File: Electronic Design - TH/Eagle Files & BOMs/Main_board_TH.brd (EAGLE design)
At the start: 90 x 60 mm, 46 parts, among them IC2 ATMEGA328-PU, X1 16MHz

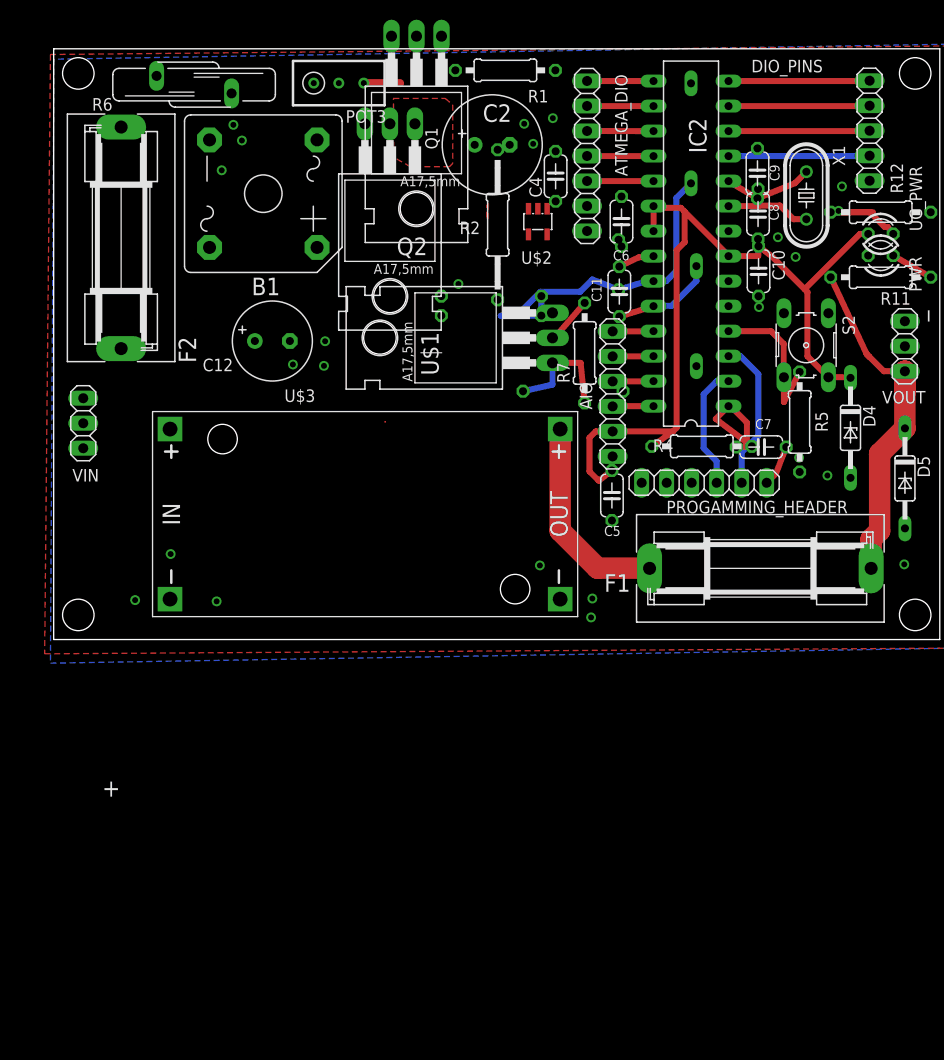
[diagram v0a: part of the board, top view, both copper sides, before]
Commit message: renamed files to reflect two versions of L.E.One and replacing ATmega 328 with arduino nano
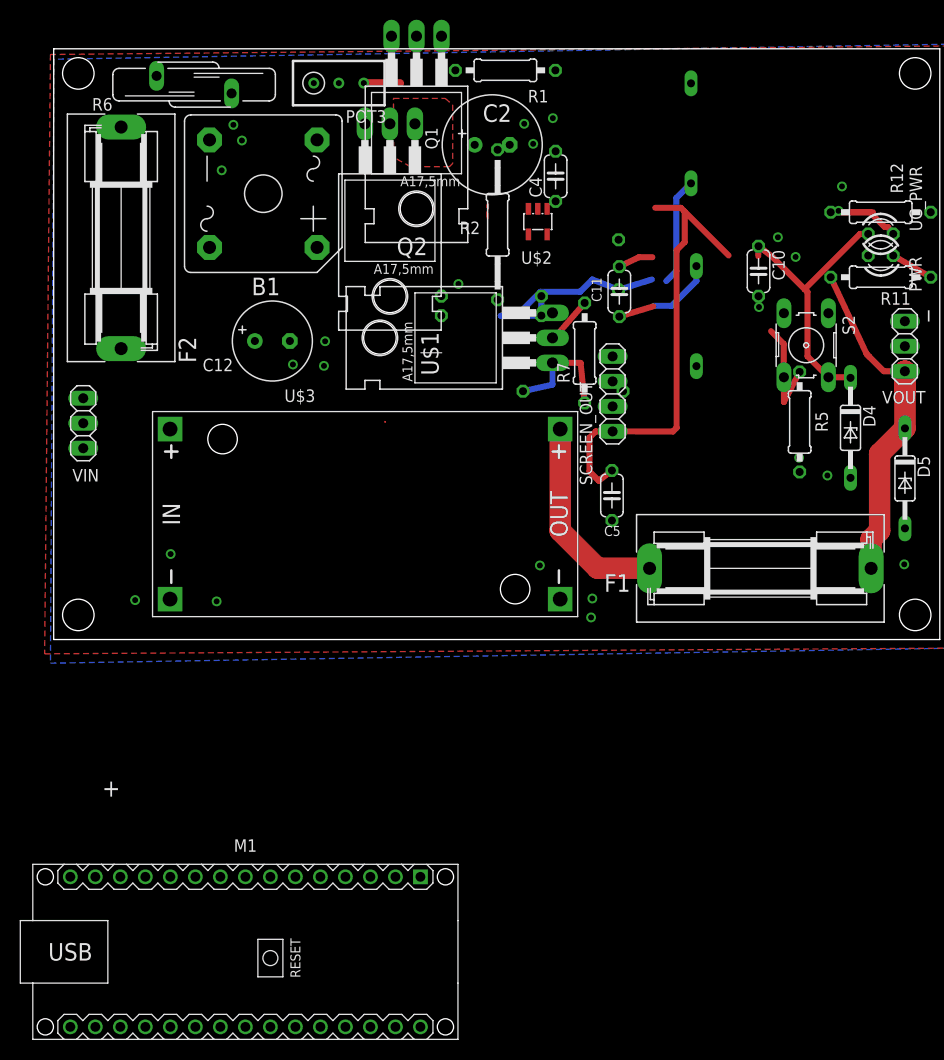
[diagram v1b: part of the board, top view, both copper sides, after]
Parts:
- removed AIO, PROGAMMING_HEADER: (no value), pinhead:1X06
- removed ATMEGA_DIO: (no value), pinhead:1X07
- removed C6, C7: 0.1u, resistor:C050-024X044
- removed C8, C9: 22p, resistor:C050-024X044
- removed DIO_PINS: (no value), pinhead:1X05
- removed IC2: ATMEGA328-PU, Arduino-AVR:DIL28-3
- removed R4: 10k, resistor:0207/10
- removed X1: 16MHz, crystal:HC49/S
- added M1: ARDUINO-NANO-3.0, diy-modules:ARDUINO-NANO-3.0
- added SCREEN_OUT: (no value), pinhead:1X04
- C10: value 0.1u -> 10u
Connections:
- removed net ANALOG_2: AIO.1, IC2.25
- removed net ANALOG_3: AIO.2, IC2.26
- removed net ANALOG_4: AIO.3, IC2.27
- removed net ANALOG_5: AIO.4, IC2.28
- removed net CRYSTAL1: C8.1, IC2.9, X1.2
- removed net CRYSTAL2: C9.1, IC2.10, X1.1
- removed net D10: ATMEGA_DIO.2, IC2.16
- removed net D11: ATMEGA_DIO.3, IC2.17
- removed net D12: ATMEGA_DIO.4, IC2.18
- removed net D13: ATMEGA_DIO.5, IC2.19
- removed net D5: DIO_PINS.2, IC2.11
- removed net D6: DIO_PINS.3, IC2.12
- removed net D7: DIO_PINS.4, IC2.13
- removed net D8: DIO_PINS.5, IC2.14
- removed net D9: ATMEGA_DIO.1, IC2.15
- removed net N$14: C7.2, PROGAMMING_HEADER.1
- removed net N$4: IC2.3, PROGAMMING_HEADER.2
- removed net N$5: IC2.2, PROGAMMING_HEADER.3
- removed net RESET: C7.1, IC2.1, R4.2
- new net 3V3: M1.J2.14
- new net 5V: M1.J2.4
- new net A2: M1.J2.10
- new net A3: M1.J2.9
- new net A6: M1.J2.6
- new net A7: M1.J2.5
- new net GND.1: M1.J1.4
- new net GND.2: M1.J2.2
- new net N$2: M1.J2.8, SCREEN_OUT.2
- new net N$3: M1.J2.7, SCREEN_OUT.1
- net +5V: now also M1.J2.1, SCREEN_OUT.3; no longer AIO.5, ATMEGA_DIO.6, C6.1, IC2.20, IC2.21, IC2.7, R4.1
- net BUTTON: now also M1.J1.5; no longer IC2.4
- net GND: now also SCREEN_OUT.4; no longer AIO.6, ATMEGA_DIO.7, C6.2, C8.2, C9.2, DIO_PINS.1, IC2.22, IC2.8, PROGAMMING_HEADER.6
- net IIN: no longer IC2.24
- net VIN: no longer IC2.23
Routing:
- net N$4: track 15.5 -> 0.00 mm
- net D7: track 14.3 -> 0.00 mm
- net D6: track 14.3 -> 0.00 mm
- net D5: track 14.3 -> 0.00 mm
- net D8: track 14.3 -> 0.00 mm
- net N$5: track 12.6 -> 0.00 mm
- net RESET: track 12.5 -> 0.00 mm
- net CRYSTAL1: track 11.6 -> 0.00 mm
- net CRYSTAL2: track 9.18 -> 0.00 mm
- net +5V: track 90.0 -> 80.9 mm
- net D11: track 6.96 -> 0.00 mm
- net D10: track 6.95 -> 0.00 mm
- net D13: track 6.95 -> 0.00 mm
- net D12: track 6.95 -> 0.00 mm
- net D9: track 6.75 -> 0.00 mm
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
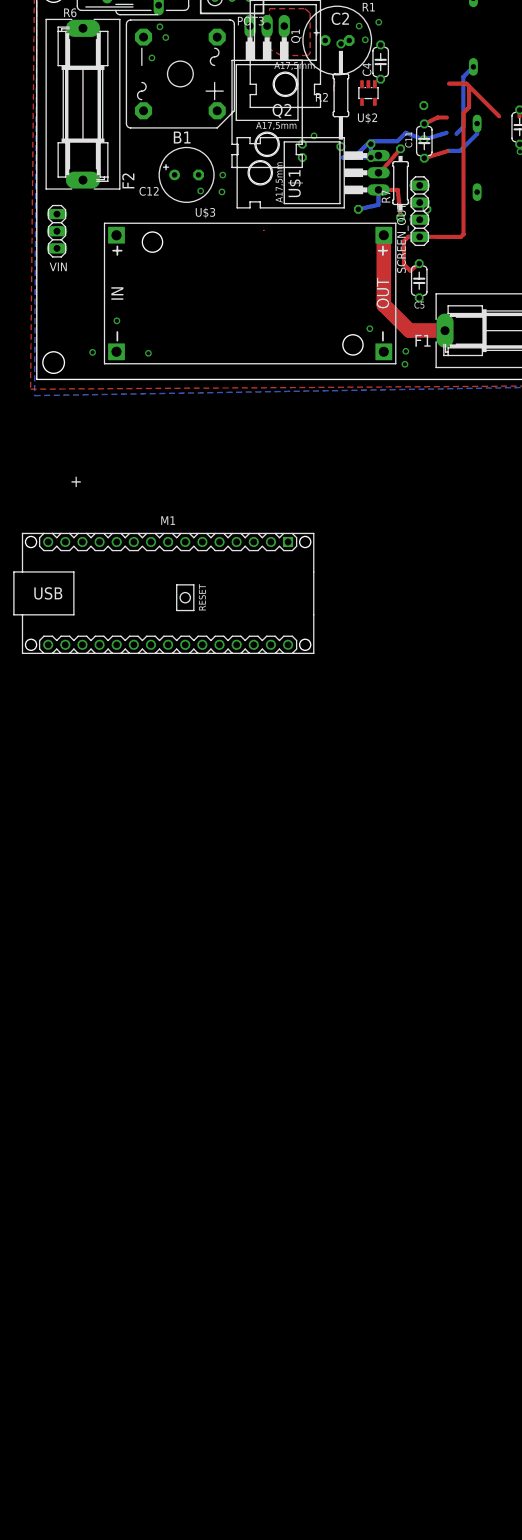
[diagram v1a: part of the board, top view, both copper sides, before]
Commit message: replacing CS30 with LM358
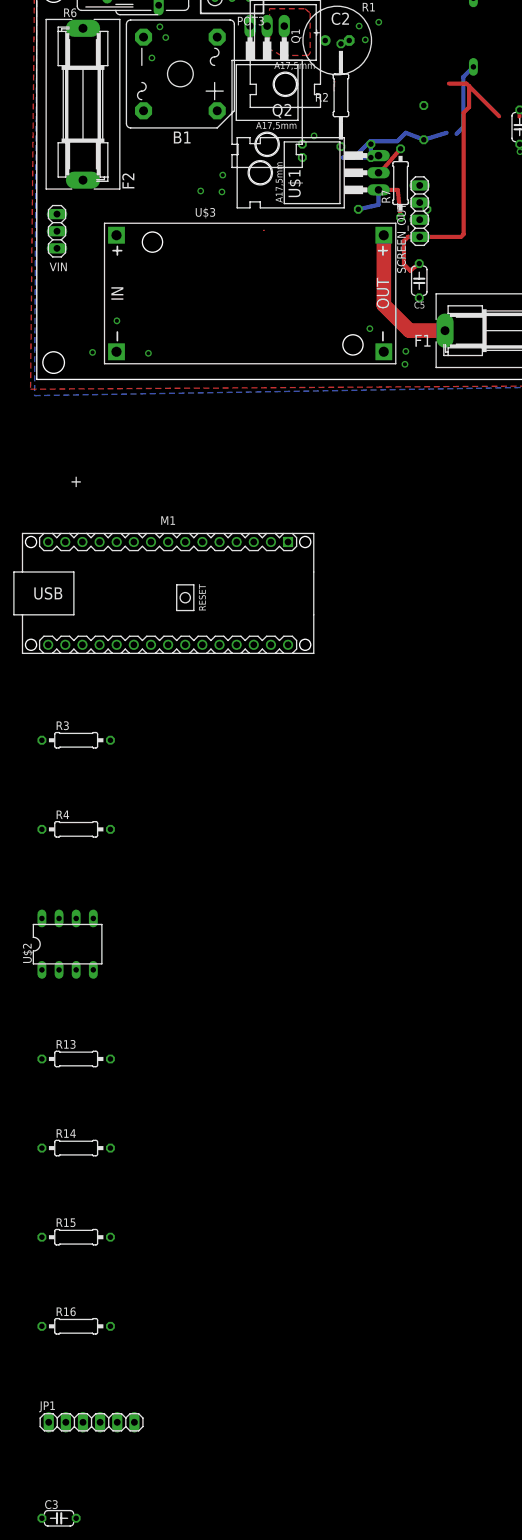
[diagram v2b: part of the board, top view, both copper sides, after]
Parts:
- removed C11: 10n, resistor:C050-024X044
- removed C12: 100uF, resistor:E3,5-8
- removed C4: 0.1u, resistor:C050-024X044
- removed D3: 5.1V, diode:DO35Z10
- added C3: 10u, resistor:C050-024X044
- added JP1: (no value), pinhead:1X06
- added R13, R16: 47k, resistor:0207/10
- added R14, R15: 10k, resistor:0207/10
- added R3, R4: 1k, resistor:0207/10
- R7: value 1k -> 220R
- R8: value 3k -> 680R
- U$2: value CS30 -> LM358; device Samson:SOT23-5L -> Samson:DIL08
- moved U$2 133.8 mm to (4.57, -83.7), turned to 0 degrees
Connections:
- removed net VIN_CURRENT_MEASURED: C12.+, R2.2, R9.2, U$1.3, U$2.4, U$3.IN+
- new net N$4: R2.2, R4.2, U$3.IN-
- new net N$5: R16.1, R4.1, U$2.3
- new net N$6: R13.2, R3.1, U$2.2
- new net N$8: R14.2, R15.1, R16.2
- net +5V: now also R15.2; no longer C4.1, U$2.5
- net A2: now also JP1.1
- net A3: now also JP1.2
- net A6: now also JP1.3
- net A7: now also JP1.4
- net GND: now also C3.2, JP1.5, JP1.6, R14.1, R2.1, R3.2, U$2.4; no longer C11.2, C12.-, C4.2, D3.A, U$2.2, U$3.IN-
- net IIN: now also M1.J2.12, R13.1; no longer C11.1, D3.C
- net VIN: now also M1.J2.11
- net VIN_PROTECTED: now also C3.1, R9.2, U$1.3, U$2.7, U$3.IN+; no longer R2.1, U$2.3
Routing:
- net IIN: track 10.5 -> 0.00 mm
- net GND: track 3.57 -> 0.00 mm

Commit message: replacing divider resistors for voltage measurement
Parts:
- R10: value 1k13 -> 1k
- R9: value 21k5 -> 10k
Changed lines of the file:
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@@
 <attribute name="VALUE" x="54.6" y="16.23" size="1.016" layer="27" rot="R270"/>
 </element>
-<element name="R9" library="resistor" package="0207/10" value="21k5" x="44.45" y="34.88" rot="MR0"/>
-<element name="R10" library="resistor" package="0207/10" value="1k13" x="44.45" y="32.9" rot="MR180"/>
+<element name="R9" library="resistor" package="0207/10" value="10k" x="44.45" y="34.88" rot="MR0"/>
+<element name="R10" library="resistor" package="0207/10" value="1k" x="44.45" y="32.9" rot="MR180"/>
 <element name="D4" library="diode" package="DO35Z10" value="5.1V" x="80.93" y="21.5" rot="R270"/>
 <element name="D5" library="diode" package="DO35Z10" value="5.1V" x="86.46" y="16.37" rot="R270"/>

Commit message: Adding names of Q1 and Q2
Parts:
- Q1, Q2: value (none) -> IRF9520
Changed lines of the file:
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@@
 <attribute name="VALUE" x="85.27" y="45.94" size="1.27" layer="27" rot="R180"/>
 </element>
-<element name="Q1" library="Samson" package="TO220BH" value="" x="36.85" y="54.93" smashed="yes" rot="R180">
+<element name="Q1" library="Samson" package="TO220BH" value="IRF9520" x="36.85" y="54.93" smashed="yes" rot="R180">
 <attribute name="NAME" x="37.735" y="52.015" size="1.27" layer="25" rot="R270"/>
 <attribute name="VALUE" x="39.055" y="58.755" size="1.27" layer="27" rot="R180"/>
 </element>
-<element name="Q2" library="Samson" package="TO220BH" value="" x="34.15" y="46.03" rot="R180"/>
+<element name="Q2" library="Samson" package="TO220BH" value="IRF9520" x="34.15" y="46.03" rot="R180"/>
 <element name="F2" library="fuse" package="SH22,5A" value="FUSESH22,5A" x="6.85" y="40.8" rot="R90">
 <attribute name="MF" value="" x="6.85" y="40.8" size="1.778" layer="27" rot="R90" display="off"/>

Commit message: adding ground to arduino
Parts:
- moved U$2 102.0 mm to (-3.81, -185.3)
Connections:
- removed net GND.2: M1.J2.2
- net GND: now also M1.J2.2
- net VIN_PROTECTED: now also U$2.8; no longer U$2.7
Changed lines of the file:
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@@
 <element name="R3" library="resistor" package="0207/10" value="1k" x="5.84" y="-53.49"/>
 <element name="R4" library="resistor" package="0207/10" value="1k" x="5.84" y="-66.7"/>
-<element name="U$2" library="Samson" package="DIL08" value="LM358" x="4.57" y="-83.72"/>
+<element name="U$2" library="Samson" package="DIL08" value="LM358" x="-3.81" y="-185.34"/>
 <element name="R13" library="resistor" package="0207/10" value="47k" x="5.84" y="-100.74"/>
 <element name="R14" library="resistor" package="0207/10" value="10k" x="5.84" y="-113.95"/>
@@
 <contactref element="JP1" pad="6"/>
 <contactref element="C3" pad="2"/>
+<contactref element="M1" pad="J2.2"/>
+<wire x1="5.84" y1="-168.83" x2="0" y2="-189.15" width="0" layer="19" extent="1-1"/>
 <wire x1="11.93" y1="-154.6" x2="5.84" y2="-168.83" width="0" layer="19" extent="1-1"/>
 <wire x1="14.47" y1="-154.6" x2="11.93" y2="-154.6" width="0" layer="19" extent="1-1"/>
 <wire x1="0.76" y1="-113.95" x2="11.93" y2="-154.6" width="0" layer="19" extent="1-1"/>
-<wire x1="8.38" y1="-87.53" x2="0.76" y2="-113.95" width="0" layer="19" extent="1-1"/>
-<wire x1="10.92" y1="-53.49" x2="8.38" y2="-87.53" width="0" layer="19" extent="1-1"/>
-<wire x1="8.2698" y1="4.00569375" x2="10.92" y2="-53.49" width="0" layer="19" extent="1-1"/>
-<wire x1="11.8798" y1="8.68569375" x2="8.2698" y2="4.00569375" width="0" layer="19" extent="1-1"/>
-<wire x1="16.5498" y1="3.87569375" x2="11.8798" y2="8.68569375" width="0" layer="19" extent="1-1"/>
-<wire x1="24.2998" y1="27.93569375" x2="11.8798" y2="8.68569375" width="0" layer="19" extent="1-1"/>
-<wire x1="27.4498" y1="27.79569375" x2="24.2998" y2="27.93569375" width="0" layer="19" extent="1-1"/>
-<wire x1="27.5698" y1="30.29569375" x2="27.4498" y2="27.79569375" width="0" layer="19" extent="1-1"/>
-<wire x1="39.37" y1="32.9" x2="27.5698" y2="30.29569375" width="0" layer="19" extent="1-1"/>
-<wire x1="41.10569375" y1="36.1102" x2="39.37" y2="32.9" width="0" layer="19" extent="1-1"/>
-<wire x1="45.09" y1="49.75" x2="41.10569375" y2="36.1102" width="0" layer="19" extent="1-1"/>
-<wire x1="46.319284375" y1="50.247296875" x2="45.09" y2="49.75" width="0" layer="19" extent="1-1"/>
-<wire x1="48.6998" y1="50.34569375" x2="46.319284375" y2="50.247296875" width="0" layer="19" extent="1-1"/>
+<wire x1="10.92" y1="-53.49" x2="0.76" y2="-113.95" width="0" layer="19" extent="1-1"/>
+<wire x1="34.71" y1="-39.34" x2="10.92" y2="-53.49" width="0" layer="19" extent="1-1"/>
+<wire x1="54.5798" y1="2.24569375" x2="34.71" y2="-39.34" width="0" layer="19" extent="1-1"/>
+<wire x1="54.7098" y1="4.16569375" x2="54.5798" y2="2.24569375" width="0" layer="19" extent="1-1"/>
+<wire x1="51.442" y1="4.104" x2="54.7098" y2="4.16569375" width="0" layer="19" extent="1-1"/>
+<wire x1="49.3798" y1="7.52569375" x2="51.442" y2="4.104" width="0" layer="19" extent="1-1"/>
+<wire x1="56.7" y1="12.09" x2="54.7098" y2="4.16569375" width="0" layer="19" extent="1-1"/>
+<wire x1="56.77" y1="21.14" x2="56.7" y2="12.09" width="0" layer="19" extent="1-1"/>
+<wire x1="57.83" y1="25.22" x2="56.77" y2="21.14" width="0" layer="19" extent="1-1"/>
+<wire x1="57.373834375" y1="40.608153125" x2="57.83" y2="25.22" width="0" layer="19" extent="1-1"/>
+<wire x1="48.6998" y1="50.34569375" x2="57.373834375" y2="40.608153125" width="0" layer="19" extent="1-1"/>
 <wire x1="47.7898" y1="52.38569375" x2="48.6998" y2="50.34569375" width="0" layer="19" extent="1-1"/>
+<wire x1="46.319284375" y1="50.247296875" x2="48.6998" y2="50.34569375" width="0" layer="19" extent="1-1"/>
+<wire x1="45.09" y1="49.75" x2="46.319284375" y2="50.247296875" width="0" layer="19" extent="1-1"/>
 <wire x1="50.6998" y1="52.95569375" x2="47.7898" y2="52.38569375" width="0" layer="19" extent="1-1"/>
 <wire x1="50.95703125" y1="57.813271875" x2="50.6998" y2="52.95569375" width="0" layer="19" extent="1-1"/>
-<wire x1="57.373834375" y1="40.608153125" x2="48.6998" y2="50.34569375" width="0" layer="19" extent="1-1"/>
 <wire x1="64.7298" y1="56.4956875" x2="50.95703125" y2="57.813271875" width="0" layer="19" extent="1-1"/>
+<wire x1="41.10569375" y1="36.1102" x2="45.09" y2="49.75" width="0" layer="19" extent="1-1"/>
+<wire x1="39.37" y1="32.9" x2="41.10569375" y2="36.1102" width="0" layer="19" extent="1-1"/>
+<wire x1="27.5698" y1="30.29569375" x2="39.37" y2="32.9" width="0" layer="19" extent="1-1"/>
+<wire x1="27.4498" y1="27.79569375" x2="27.5698" y2="30.29569375" width="0" layer="19" extent="1-1"/>
+<wire x1="24.2998" y1="27.93569375" x2="27.4498" y2="27.79569375" width="0" layer="19" extent="1-1"/>
 <wire x1="71.59" y1="34.87" x2="57.373834375" y2="40.608153125" width="0" layer="19" extent="1-1"/>
 <wire x1="71.63569375" y1="33.7702" x2="71.59" y2="34.87" width="0" layer="19" extent="1-1"/>
@@
 <wire x1="86.45" y1="32.33" x2="82.73" y2="39" width="0" layer="19" extent="1-1"/>
 <wire x1="89.08" y1="43.4" x2="82.73" y2="39" width="0" layer="19" extent="1-1"/>
-<wire x1="57.83" y1="25.22" x2="57.373834375" y2="40.608153125" width="0" layer="19" extent="1-1"/>
-<wire x1="56.77" y1="21.14" x2="57.83" y2="25.22" width="0" layer="19" extent="1-1"/>
-<wire x1="56.7" y1="12.09" x2="56.77" y2="21.14" width="0" layer="19" extent="1-1"/>
-<wire x1="54.7098" y1="4.16569375" x2="56.7" y2="12.09" width="0" layer="19" extent="1-1"/>
-<wire x1="54.5798" y1="2.24569375" x2="54.7098" y2="4.16569375" width="0" layer="19" extent="1-1"/>
-<wire x1="51.442" y1="4.104" x2="54.7098" y2="4.16569375" width="0" layer="19" extent="1-1"/>
-<wire x1="49.3798" y1="7.52569375" x2="51.442" y2="4.104" width="0" layer="19" extent="1-1"/>
 <wire x1="75.7098" y1="18.46569375" x2="71.63569375" y2="33.7702" width="0" layer="19" extent="1-1"/>
 <wire x1="75.765540625" y1="17.022259375" x2="75.7098" y2="18.46569375" width="0" layer="19" extent="1-1"/>
@@
 <wire x1="15.828996875" y1="50.746584375" x2="18.2498" y2="52.27569375" width="0" layer="19" extent="1-1"/>
 <wire x1="17.06569375" y1="47.6602" x2="15.828996875" y2="50.746584375" width="0" layer="19" extent="1-1"/>
+<wire x1="11.8798" y1="8.68569375" x2="24.2998" y2="27.93569375" width="0" layer="19" extent="1-1"/>
+<wire x1="8.2698" y1="4.00569375" x2="11.8798" y2="8.68569375" width="0" layer="19" extent="1-1"/>
+<wire x1="16.5498" y1="3.87569375" x2="11.8798" y2="8.68569375" width="0" layer="19" extent="1-1"/>
 </signal>
 <signal name="VIN_PROTECTED">
@@
 <contactref element="U$1" pad="3"/>
 <contactref element="R9" pad="2"/>
-<contactref element="U$2" pad="7"/>
+<contactref element="U$2" pad="8"/>
 <contactref element="C3" pad="1"/>
-<wire x1="3.3" y1="-79.91" x2="0.76" y2="-168.83" width="0" layer="19" extent="1-1"/>
-<wire x1="11.818" y1="21.376" x2="3.3" y2="-79.91" width="0" layer="19" extent="1-1"/>
+<wire x1="-7.62" y1="-181.53" x2="0.76" y2="-168.83" width="0" layer="19" extent="1-1"/>
+<wire x1="11.818" y1="21.376" x2="-7.62" y2="-181.53" width="0" layer="19" extent="1-1"/>
 <wire x1="39.37" y1="34.88" x2="11.818" y2="21.376" width="0" layer="19" extent="1-1"/>
 <wire x1="50.66" y1="33.18" x2="39.37" y2="34.88" width="0" layer="19" extent="1-1"/>
@@
 <contactref element="M1" pad="J1.4"/>
 </signal>
-<signal name="GND.2">
-<contactref element="M1" pad="J2.2"/>
-</signal>
 <signal name="5V">
 <contactref element="M1" pad="J2.4"/>
@@
 <contactref element="R13" pad="1"/>
 <contactref element="U$2" pad="1"/>
-<wire x1="0.76" y1="-87.53" x2="0.76" y2="-100.74" width="0" layer="19" extent="1-1"/>
-<wire x1="9.31" y1="-39.34" x2="0.76" y2="-87.53" width="0" layer="19" extent="1-1"/>
+<wire x1="-7.62" y1="-189.15" x2="0.76" y2="-100.74" width="0" layer="19" extent="1-1"/>
+<wire x1="9.31" y1="-39.34" x2="-7.62" y2="-189.15" width="0" layer="19" extent="1-1"/>
 </signal>
 <signal name="N$5">
@@
 <contactref element="U$2" pad="3"/>
 <contactref element="R16" pad="1"/>
-<wire x1="5.84" y1="-87.53" x2="0.76" y2="-140.37" width="0" layer="19" extent="1-1"/>
-<wire x1="0.76" y1="-66.7" x2="5.84" y2="-87.53" width="0" layer="19" extent="1-1"/>
+<wire x1="-2.54" y1="-189.15" x2="0.76" y2="-140.37" width="0" layer="19" extent="1-1"/>
+<wire x1="0.76" y1="-66.7" x2="-2.54" y2="-189.15" width="0" layer="19" extent="1-1"/>
 </signal>
 <signal name="N$6">
@@
 <contactref element="U$2" pad="2"/>
 <contactref element="R13" pad="2"/>
-<wire x1="3.3" y1="-87.53" x2="10.92" y2="-100.74" width="0" layer="19" extent="1-1"/>
-<wire x1="0.76" y1="-53.49" x2="3.3" y2="-87.53" width="0" layer="19" extent="1-1"/>
+<wire x1="-5.08" y1="-189.15" x2="10.92" y2="-100.74" width="0" layer="19" extent="1-1"/>
+<wire x1="0.76" y1="-53.49" x2="-5.08" y2="-189.15" width="0" layer="19" extent="1-1"/>
 </signal>
 <signal name="N$8">
